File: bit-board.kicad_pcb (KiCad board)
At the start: 2 copper layers, 85.6 x 56 mm, 202 parts, among them M1 FDV301N, M1A NX3008PBK, M1B2 FDV301N, M1B3 FDV301N, M1BF NX3008PBK, M1BG NX3008PBK, M1DE FDV301N, M1L0 FDV301N, M1L1 FDV301N, M1L2 FDV301N, M1L3 FDV301N, M1MAG FDV301N, M1NAF FDV301N, M1NAG FDV301N, M1NEE FDV301N, M1NL FDV301N, M1NS4 FDV301N, M1OEE FDV301N, M1ON FDV301N, M1S5 FDV301N, M1S6 FDV301N, M1S7 FDV301N, M1S8 FDV301N, M1S9 FDV301N, M1XE FDV301N, M2 FDV301N, M2A FDV301N, M2B2 NX3008PBK, M2B3 NX3008PBK, M2BF FDV301N, M2BG FDV301N, M2DE FDV301N, M2L0 FDV301N, M2L1 FDV301N, M2L2 FDV301N, M2L3 FDV301N, M2MAG FDV301N, M2NAF FDV301N, M2NAG FDV301N, M2NEE FDV301N, M2NL FDV301N, M2NS4 FDV301N, M2OEE FDV301N, M2ON FDV301N, M2S5 FDV301N, M2S6 FDV301N, M2S7 FDV301N, M2S8 FDV301N, M2S9 FDV301N, M2XE FDV301N, M3 FDV301N, M3A NX3008PBK, M3BF NX3008PBK, M3BG NX3008PBK, M3OEE FDV301N, M3ON FDV301N, M3XE FDV301N, M4 FDV301N, M4A FDV301N, M4BF FDV301N, M4BG FDV301N, M4XE FDV301N, Q1BF PDTC124TU, Q1BG PDTC124TU, Q1K PDTC124TU, Q1L0 PDTC124TU, Q1L1 PDTC124TU, Q1L2 PDTC124TU, Q1L3 PDTC124TU, Q1R PDTC124TU, Q1U PDTC124TU, Q1X PDTC124TU, Q1Y PDTC124TU, Q2A PDTC124TU, Q2BF PDTC124TU, Q2BG PDTC124TU, Q2K PDTC124TU, Q2L0 PDTC124TU, Q2L1 PDTC124TU, Q2L2 PDTC124TU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

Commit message: Bit board mostly routed.
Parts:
- added JMAIN: unknown, Parts:pci-edge-3v, F.Cu at (143.0, 101.1)
- moved RPS4 113.6 mm to (105.2, 89.0), turned to -90 degrees
- moved RNS4 106.4 mm to (110.0, 61.0), turned to 90 degrees
- moved RS6 101.8 mm to (114.8, 74.0), turned to -90 degrees
- moved RIS4 98.9 mm to (115.2, 86.0), turned to 90 degrees
- moved RI3 93.0 mm to (114.8, 62.0), turned to 90 degrees
- moved R5 92.8 mm to (122.5, 88.2)
- moved D5 91.5 mm to (120.0, 66.8), turned to 90 degrees
- moved D4 65.0 mm to (150.1, 52.5), turned to -90 degrees
- moved RON 60.0 mm to (159.8, 81.5), turned to 180 degrees
- moved R4 55.7 mm to (162.6, 53.2), turned to 180 degrees
- moved RI4 53.3 mm to (154.8, 52.1), turned to -90 degrees
- moved RPE 52.4 mm to (171.8, 90.9)
- moved RNN 44.6 mm to (169.8, 62.0), turned to 90 degrees
- moved RMAG 39.5 mm to (175.2, 57.0), turned to 90 degrees
- moved D3 39.4 mm to (122.5, 86.5)
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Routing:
- net Vdd: track 0.00 -> 348.0 mm, vias 0 -> 23
- net phi: track 0.00 -> 127.8 mm, vias 0 -> 7
- net Ao#: track 0.00 -> 72.7 mm, vias 0 -> 2
- net W#: track 0.00 -> 62.2 mm, vias 0 -> 7
- net SB: track 0.00 -> 58.2 mm, vias 0 -> 3
- net Bi#: track 0.00 -> 54.4 mm, vias 0 -> 7
- net B#: track 0.00 -> 51.0 mm, vias 0 -> 4
- net W: track 0.00 -> 49.0 mm, vias 0 -> 6
- net VPush: track 0.00 -> 48.4 mm, vias 0 -> 1
- net N#: track 0.00 -> 48.3 mm, vias 0 -> 2
- net WA: track 0.00 -> 46.1 mm, vias 0 -> 2
- net S2: track 0.00 -> 45.3 mm, vias 0 -> 2
- net S3: track 0.00 -> 45.1 mm, vias 0 -> 2
- net B: track 0.00 -> 44.1 mm, vias 0 -> 2
- net I#: track 0.00 -> 43.9 mm, vias 0 -> 1
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- added copper zone on In1.Cu, net GND
- added copper zone on In2.Cu, net GND
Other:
- copper layers 2 -> 4
- board text added: "A"
- board text added: "K"
- board text added: "PC"
- board text added: "R"
- board text added: "U"
- board text added: "X"
- board text added: "Y"

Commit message: About to sort out silkscreen....
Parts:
- moved C9 100.2 mm to (104.5, 55.0)
- moved C13 99.5 mm to (105.2, 84.0), turned to 90 degrees
- moved C14 99.4 mm to (105.2, 74.0), turned to 90 degrees
- moved C10 89.4 mm to (116.0, 55.5), turned to 90 degrees
- moved C11 80.5 mm to (126.0, 55.5), turned to 90 degrees
- moved C12 71.3 mm to (136.0, 55.5), turned to 90 degrees
- moved C6 64.3 mm to (139.3, 88.8)
- moved C8 63.1 mm to (140.8, 61.0), turned to -90 degrees
- moved C2 59.7 mm to (139.5, 69.0)
- moved C5 59.5 mm to (139.4, 83.8)
- moved C3 59.5 mm to (139.4, 74.2)
- moved C4 59.4 mm to (139.5, 79.0)
- moved C7 57.1 mm to (145.7, 64.5), turned to 180 degrees
- moved C17 55.8 mm to (155.7, 54.5), turned to 180 degrees
- moved C16 32.9 mm to (174.8, 69.5), turned to 180 degrees
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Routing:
- net Pp#: track 10.2 -> 33.0 mm, vias 0 -> 3
- net AR#: track 0.00 -> 17.6 mm, vias 0 -> 1
- net GND: track 42.2 -> 56.7 mm, vias 51 -> 72
- net Ao#: track 72.7 -> 62.4 mm, vias 2 -> 3
- net P#: track 13.1 -> 23.0 mm
- net CR: track 0.00 -> 8.52 mm, vias 0 -> 1
- net W#: track 62.2 -> 53.9 mm, vias 7 -> 6
- net N#: track 48.3 -> 40.5 mm, vias 2 -> 1
- net WA: track 46.1 -> 39.2 mm
- net gl_A: track 18.5 -> 13.1 mm, vias 2 -> 0
- net Ci#: track 25.2 -> 30.3 mm, vias 2 -> 3
- net Bi#: track 54.4 -> 50.1 mm
- net m_O_E_E: track 0.00 -> 4.05 mm
- net x_O_N: track 12.3 -> 9.05 mm, vias 3 -> 2
- net R_G: track 22.7 -> 19.7 mm, vias 3 -> 2
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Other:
- board size 85.6 x 56 mm -> 85 x 56 mm
- board text added: "+1"
- board text added: "Arithmetic Unit"
- board text added: "Branch"
- board text added: "Instruction"
- board text added: "S0"
- board text added: "S1"
- board text added: "S2"
- board text added: "S3"
- board text added: "Stack"

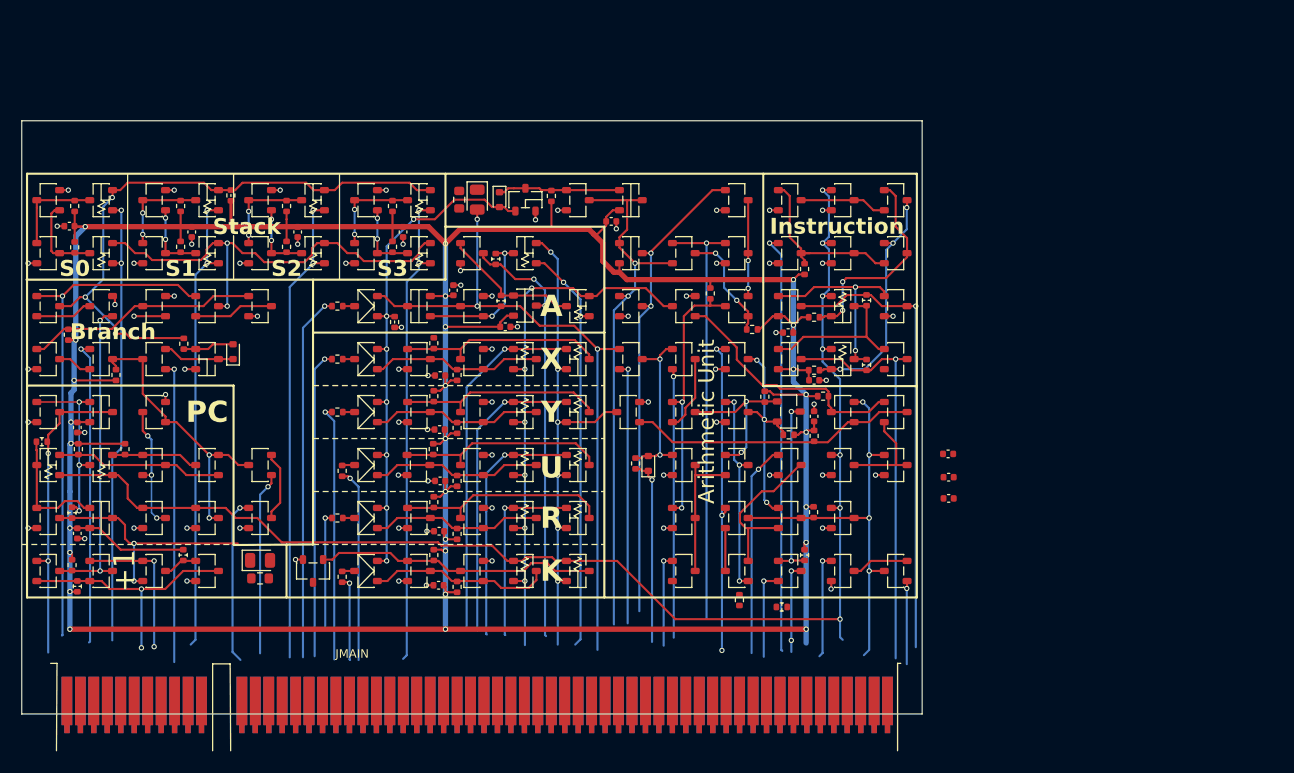
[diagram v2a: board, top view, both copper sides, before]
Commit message: Silkscreen sorted, and a little DRC clean-up.
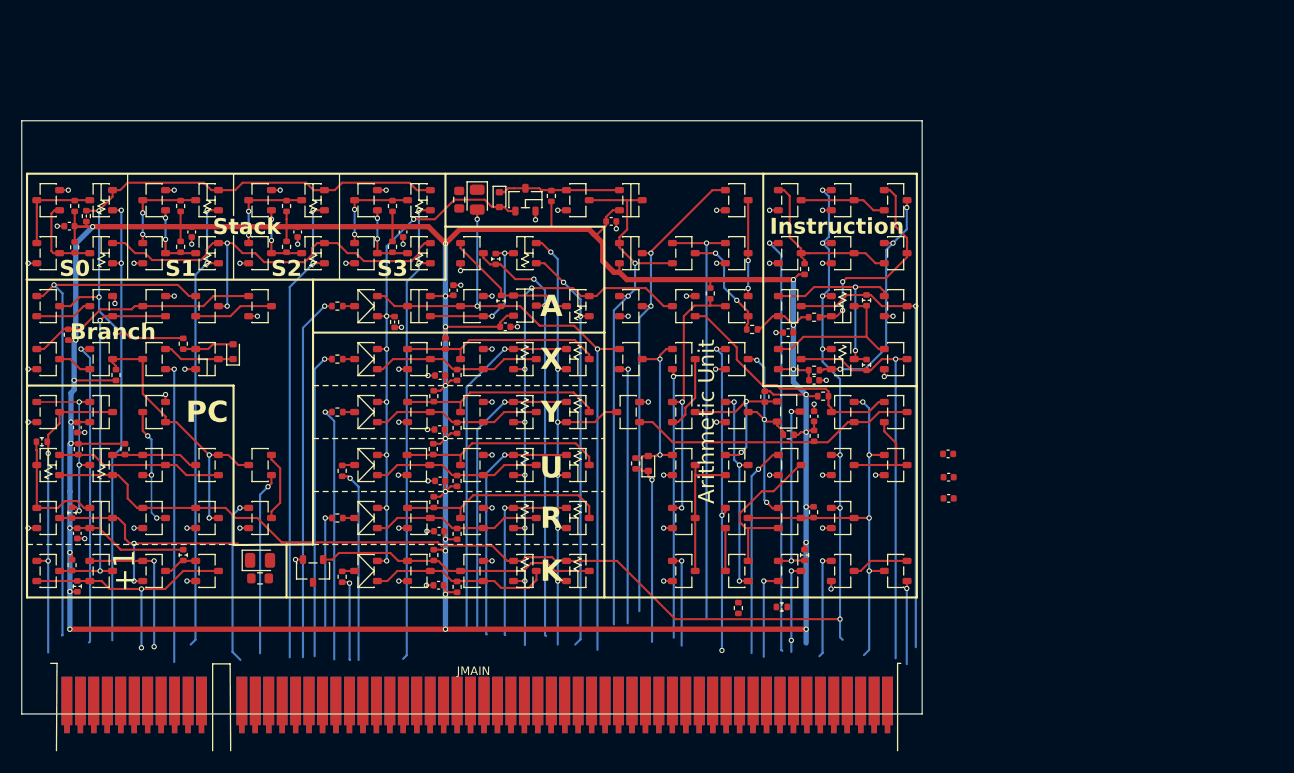
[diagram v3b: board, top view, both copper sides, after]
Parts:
- moved R2 13.8 mm to (106.1, 54.0)
- moved RJX 1.10 mm to (140.0, 66.0)
- moved RXE 0.76 mm to (167.7, 91.0)
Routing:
- net Pp#: track 33.0 -> 35.0 mm, vias 3 -> 2
- net SB: track 56.9 -> 58.3 mm
- net GND: track 56.7 -> 58.1 mm, vias 72 -> 74
- net VPush: track 47.9 -> 49.3 mm

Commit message: Separate the double diodes.
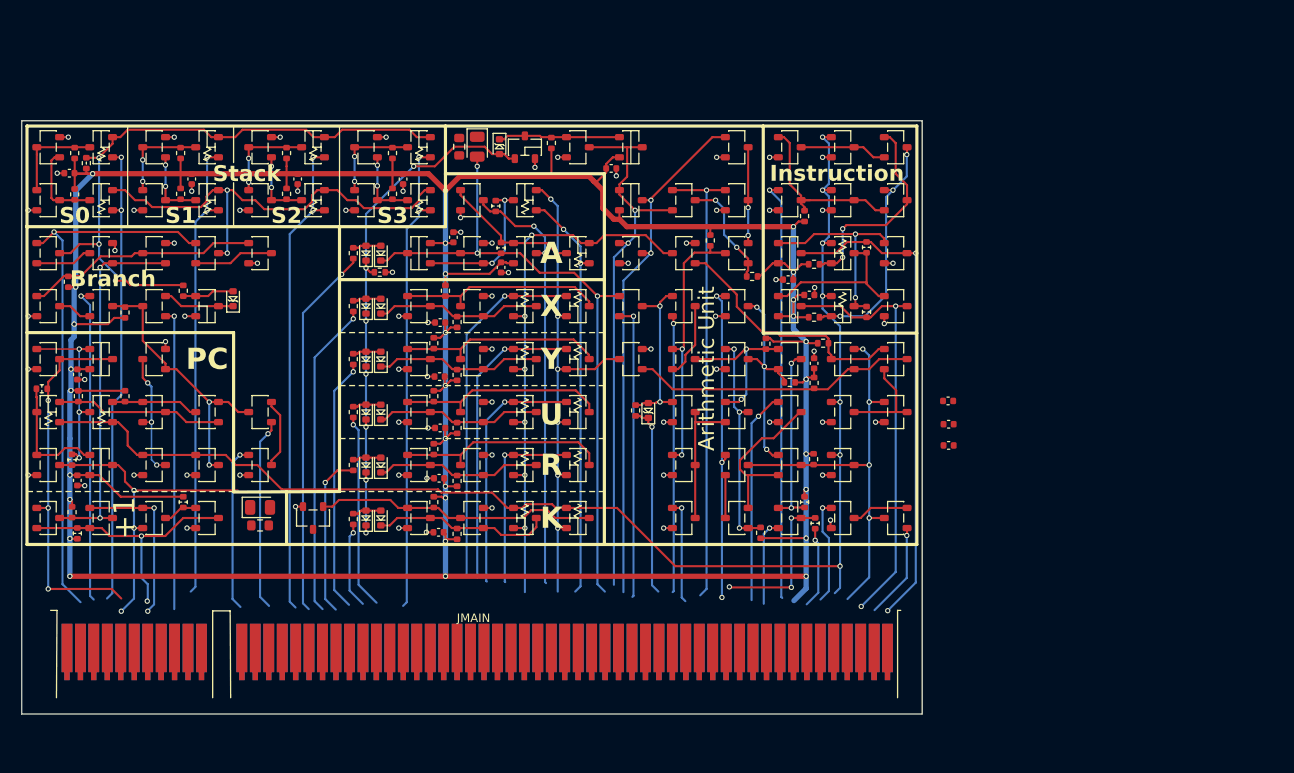
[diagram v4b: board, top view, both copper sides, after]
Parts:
- removed DA, DK, DR, DU, DX, DY: unknown, Parts:sot23-baw56
- added D1A: 1N4148WT, Parts:SOD523-diode, F.Cu at (132.5, 57.5)
- added D1K: 1N4148WT, Parts:SOD523-diode, F.Cu at (132.5, 82.5)
- added D1R: 1N4148WT, Parts:SOD523-diode, F.Cu at (132.5, 77.5)
- added D1U: 1N4148WT, Parts:SOD523-diode, F.Cu at (132.5, 72.5)
- added D1X: 1N4148WT, Parts:SOD523-diode, F.Cu at (132.5, 62.5)
- added D1Y: 1N4148WT, Parts:SOD523-diode, F.Cu at (132.5, 67.5)
- added D2A: 1N4148WT, Parts:SOD523-diode, F.Cu at (133.9, 57.5)
- added D2K: 1N4148WT, Parts:SOD523-diode, F.Cu at (133.9, 82.5)
- added D2R: 1N4148WT, Parts:SOD523-diode, F.Cu at (133.9, 77.5)
- added D2U: 1N4148WT, Parts:SOD523-diode, F.Cu at (133.9, 72.5)
- added D2X: 1N4148WT, Parts:SOD523-diode, F.Cu at (133.9, 62.5)
- added D2Y: 1N4148WT, Parts:SOD523-diode, F.Cu at (133.9, 67.5)
- D1, D4, D5: footprint Parts:SOD523 -> Parts:SOD523-schottky
- moved RPE 8.50 mm to (174.9, 83.0), turned to -90 degrees
- moved C16 8.06 mm to (174.3, 61.5)
- moved RXE 7.40 mm to (169.8, 83.9)
- moved RS6 5.96 mm to (109.8, 63.1)
- moved R1U 5.65 mm to (131.3, 72.5)
- moved C7 5.61 mm to (145.2, 58.9), turned to 90 degrees
- moved R1K 5.55 mm to (131.3, 82.6)
- moved R1R 5.22 mm to (131.3, 77.5), turned to 90 degrees
- moved R1X 5.22 mm to (131.3, 62.5), turned to 90 degrees
- moved R1Y 5.22 mm to (131.3, 67.5), turned to 90 degrees
- moved R3A 5.22 mm to (131.3, 57.5), turned to 90 degrees
- moved M3 5.01 mm to (157.5, 67.5)
- moved RDE 5.00 mm to (170.2, 66.0)
- moved MIU 5.00 mm to (137.5, 72.5)
- moved RJU 5.00 mm to (138.9, 71.0)
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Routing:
- net Vdd: track 345.5 -> 353.8 mm, vias 27 -> 29
- net P#: track 23.0 -> 31.1 mm, vias 2 -> 3
- net CS#: track 0.00 -> 7.72 mm, vias 0 -> 1
- net P: track 29.2 -> 35.5 mm, vias 2 -> 3
- net Co#: track 8.57 -> 14.7 mm, vias 2 -> 3
- net RR: track 11.0 -> 15.5 mm
- net B: track 45.5 -> 49.3 mm
- net N#: track 40.5 -> 43.5 mm
- net AS: track 24.8 -> 27.9 mm
- net I#: track 43.9 -> 46.5 mm, vias 1 -> 2
- net VPush: track 49.3 -> 51.9 mm
- net PCi: track 14.2 -> 16.1 mm
- net br_X: track 1.12 -> 2.68 mm
- net br_A: track 1.12 -> 2.68 mm
- net br_Y: track 1.12 -> 2.68 mm
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
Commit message: Route the bit board connector.  DRC clean.
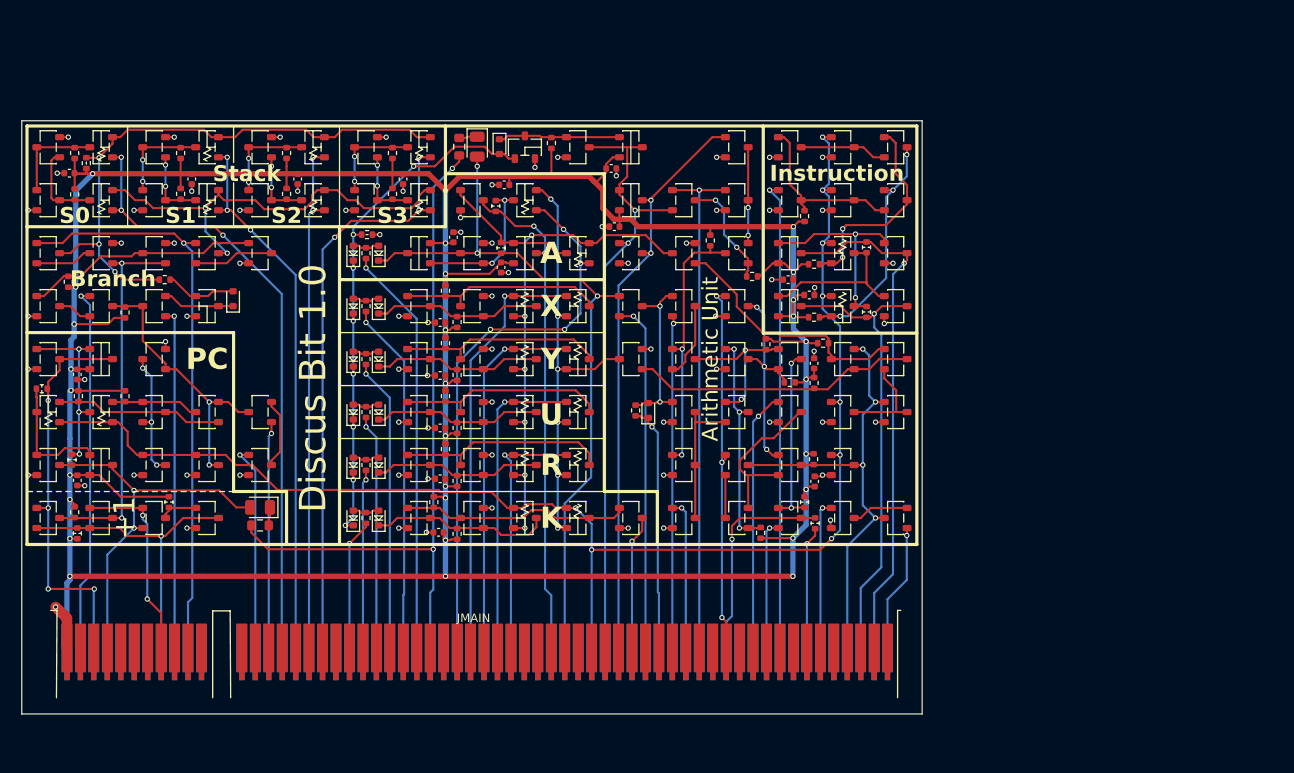
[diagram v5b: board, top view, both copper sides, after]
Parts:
- D1, D4, D5: footprint Parts:SOD523-schottky -> Parts:SOD523
- moved C19 47.7 mm to (145.6, 51.0)
- moved C18 35.5 mm to (155.9, 55.0)
- moved M4 30.0 mm to (157.5, 82.5), turned to 0 degrees
- moved C20 13.1 mm to (174.8, 79.0), turned to -90 degrees
- moved R1 3.75 mm to (132.6, 55.8)
- moved R6 2.04 mm to (113.5, 60.0), turned to 180 degrees
- moved RIS4 1.35 mm to (113.9, 81.0)
- moved R1K 1.20 mm to (132.5, 82.5)
- moved D1A 1.20 mm to (131.3, 57.5)
- moved D1K 1.20 mm to (131.3, 82.5)
- moved D1R 1.20 mm to (131.3, 77.5)
- moved D1U 1.20 mm to (131.3, 72.5)
- moved D1X 1.20 mm to (131.3, 62.5)
- moved D1Y 1.20 mm to (131.3, 67.5)
- moved R1R 1.20 mm to (132.5, 77.5)
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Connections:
- D3 pad 1: Bling -> _d3
- D3 pad 2: _d3 -> P#
- JMAIN pad A10: (no net) -> VPush
- JMAIN pad A14: S0 -> (no net)
- JMAIN pad A15: S1 -> Jump
- JMAIN pad A16: S2 -> J
- JMAIN pad A17: S3 -> S0
- JMAIN pad A18: PCo -> S1
- JMAIN pad A19: (no net) -> S2
- JMAIN pad A2: O -> Inc
- JMAIN pad A20: P -> S3
- JMAIN pad A22: WA -> RK
- JMAIN pad A23: (no net) -> RR
- JMAIN pad A24: WX -> RU
- JMAIN pad A25: (no net) -> RY
- JMAIN pad A26: WY -> RX
- JMAIN pad A27: (no net) -> RA
- JMAIN pad A28: WU -> Bling
- JMAIN pad A3: J -> P
- JMAIN pad A30: Ao -> WA
- JMAIN pad A31: Z -> WX
- JMAIN pad A32: phi -> WY
- JMAIN pad A33: (no net) -> WU
- JMAIN pad A34: Bling -> WR
- JMAIN pad A35: K# -> (no net)
- JMAIN pad A37: (no net) -> Ao
- JMAIN pad A38: (no net) -> Ao#
- JMAIN pad A4: I -> P#
- JMAIN pad A40: B -> phi
- JMAIN pad A41: (no net) -> B#
- JMAIN pad A42: (no net) -> B
- JMAIN pad A43: (no net) -> Z
- JMAIN pad A44: (no net) -> AS
- JMAIN pad A45: (no net) -> AR#
- JMAIN pad A46: (no net) -> OR
- JMAIN pad A47: (no net) -> AND
- JMAIN pad A48: (no net) -> N#
- JMAIN pad A5: I# -> (no net)
- JMAIN pad A51: N# -> (no net)
- JMAIN pad A52: AS -> QE
- JMAIN pad A53: AR# -> CR
- JMAIN pad A54: OR -> O
- JMAIN pad A55: AND -> (no net)
- JMAIN pad A57: CR -> CON
- JMAIN pad A58: QE -> (no net)
- JMAIN pad A6: Inc -> (no net)
- JMAIN pad A60: WR -> I
- JMAIN pad A61: (no net) -> I#
- JMAIN pad A62: (no net) -> K#
- JMAIN pad A7: Jump -> (no net)
- JMAIN pad A8: Ret -> PCo
- JMAIN pad A9: VPush -> Ret
- JMAIN pad B18: PCi -> (no net)
- JMAIN pad B20: P# -> (no net)
- JMAIN pad B22: RA -> (no net)
- JMAIN pad B24: RX -> (no net)
- JMAIN pad B26: RY -> (no net)
- JMAIN pad B28: RU -> (no net)
- JMAIN pad B29: RK -> (no net)
- JMAIN pad B30: Ao# -> (no net)
- JMAIN pad B39: CON -> (no net)
- JMAIN pad B40: B# -> (no net)
- JMAIN pad B60: RR -> (no net)
- JMAIN pad B8: (no net) -> PCi
- R5 pad 1: P# -> _d3
- R5 pad 2: _d3 -> Bling
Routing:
- net Bling: track 0.00 -> 66.1 mm, vias 0 -> 2
- net S0: track 43.9 -> 58.5 mm, vias 2 -> 3
- net WA: track 39.2 -> 53.3 mm, vias 2 -> 4
- net Z: track 0.00 -> 12.7 mm, vias 0 -> 1
- net S3: track 45.1 -> 55.4 mm, vias 2 -> 3
- net S1: track 43.8 -> 50.9 mm, vias 2 -> 3
- net GND: track 58.2 -> 65.1 mm, vias 74 -> 77
- net WX: track 33.9 -> 40.4 mm
- net Ao#: track 61.8 -> 68.3 mm
- net WR: track 17.8 -> 24.2 mm
- net WY: track 28.5 -> 34.8 mm
- net Ao: track 41.0 -> 47.4 mm
- net B#: track 52.4 -> 58.7 mm
- net W#: track 53.9 -> 47.9 mm
- net W: track 49.3 -> 43.3 mm
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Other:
- board text added: "Discus Bit 1.0"

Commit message: Tidy silkscreen a bit.
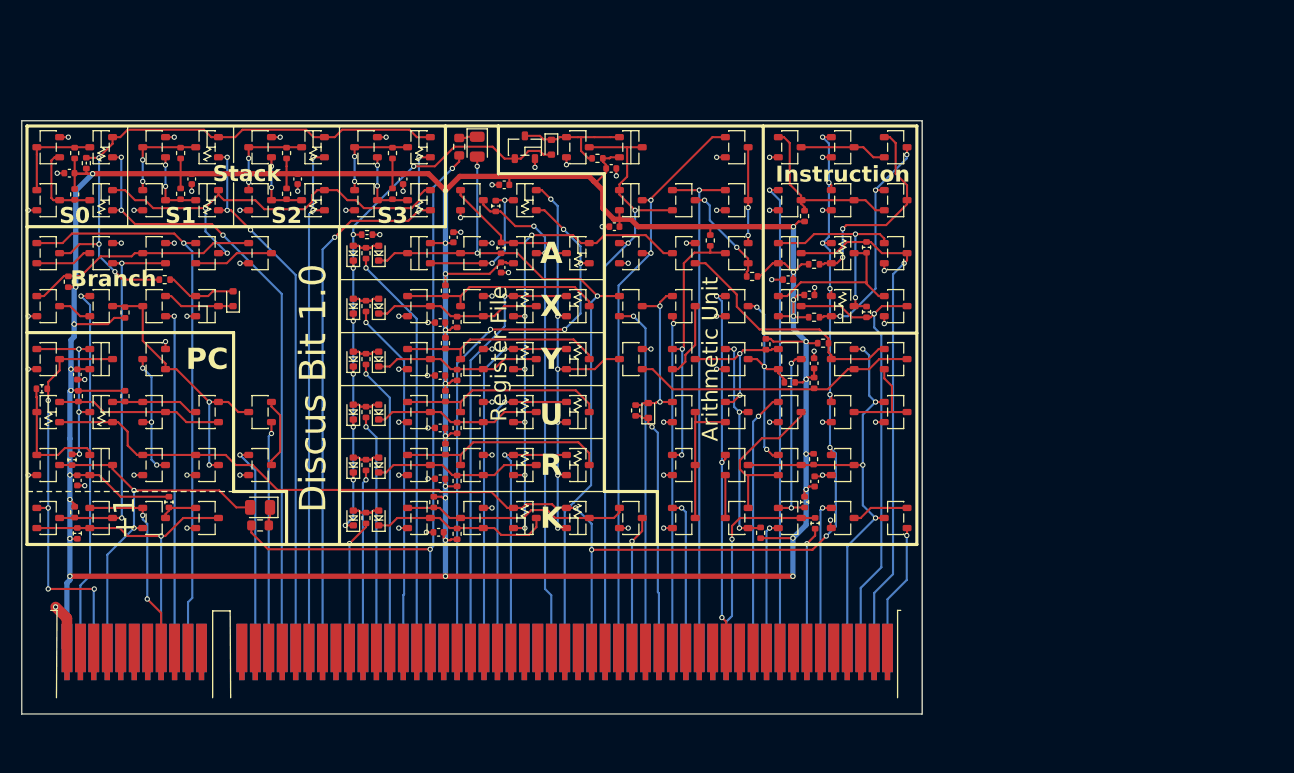
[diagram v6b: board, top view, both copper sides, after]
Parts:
- moved D4 4.90 mm to (150.0, 47.5)
- moved RI4 4.59 mm to (154.3, 48.5), turned to 0 degrees
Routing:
- net Bi#: track 52.4 -> 56.3 mm
- net Vdd: track 354.0 -> 352.1 mm
- net phi: track 134.9 -> 133.4 mm
- net Q_D_E: track 14.7 -> 13.8 mm
- net x_N: track 10.5 -> 9.85 mm
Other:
- board text added: "Register File"
